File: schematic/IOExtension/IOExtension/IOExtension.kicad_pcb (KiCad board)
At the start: 2 copper layers, 73.4 x 72.4 mm, 32 parts, among them J1 Address, J10 Opto_GPB2, J11 Opto_GPB3, J12 IO_GPB, J13 Opto_GPB4, J14 OLED_SCR, J2 TTL Serial OUT, J3 PORT_C_IN, J4 PORT_C_OUT, J5 INTs/Ts, J6 TTL Serial IN, J7 INTs/Ts, J8 IO_GPA, J9 Opto_IN, U1 MCP23017_SP, U2 4N25, U3 4N25, U4 4N25

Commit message: Latest shcematic of IOExtesion board and latest Gerbers
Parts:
- added GND: MountingHole_2.2mm_M2_ISO7380_Pad, MountingHole:MountingHole_2.2mm_M2_ISO7380_Pad, F.Cu at (111.5, 108.5)
- added GND: MountingHole_2.2mm_M2_ISO7380_Pad, MountingHole:MountingHole_2.2mm_M2_ISO7380_Pad, F.Cu at (132.5, 108.5)
- added R12: 1K, Resistor_THT:R_Axial_DIN0204_L3.6mm_D1.6mm_P7.62mm_Horizontal, F.Cu at (126.0, 96.9)
- added R13: 1K, Resistor_THT:R_Axial_DIN0204_L3.6mm_D1.6mm_P7.62mm_Horizontal, F.Cu at (123.5, 96.9)
- added SW1: B_USER1, Button_Switch_THT:SW_PUSH_6mm_H5mm, F.Cu at (131.5, 73.0)
- added U5: 24LC512, Package_DIP:DIP-8_W7.62mm, F.Cu at (83.2, 94.2)
- moved J14 32.4 mm to (118.4, 87.0), turned to 90 degrees
- moved J9 6.20 mm to (136.0, 67.1)
- moved R1 5.00 mm to (102.3, 98.5)
- moved R3 5.00 mm to (102.3, 93.5)
- moved C4 3.16 mm to (106.0, 81.5)
- moved J8 2.29 mm to (138.0, 82.0)
- moved J1 1.96 mm to (101.0, 102.0)
- moved J12 1.88 mm to (73.5, 101.3)
- moved R11 1.57 mm to (117.6, 77.5)
- moved R4 1.50 mm to (85.6, 78.0)
- moved J13 1.46 mm to (84.0, 69.0)
- moved J10 1.42 mm to (89.5, 60.0)
- moved J11 1.42 mm to (89.5, 69.0)
- moved D1 1.27 mm to (72.8, 78.0)
- moved U4 1.22 mm to (117.7, 69.5)
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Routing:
- net /SCK: track 61.2 -> 101.8 mm, vias 1 -> 2
- net /SDA: track 66.6 -> 104.6 mm
- net Net-(J8-Pin_1): track 53.1 -> 64.1 mm
- net +5V: track 320.9 -> 329.8 mm
- net Net-(J9-Pin_1): track 31.7 -> 38.5 mm
- net Net-(J1-Pin_5): track 19.4 -> 15.8 mm
- net /GPB3_OPTO: track 51.5 -> 54.4 mm
- net Net-(J1-Pin_3): track 21.1 -> 18.3 mm
- net Net-(J1-Pin_1): track 23.0 -> 20.4 mm
- net Net-(J9-Pin_3): track 29.4 -> 27.0 mm
- net /GPB4_DIR: track 39.6 -> 37.2 mm
- net Net-(J8-Pin_8): track 46.9 -> 49.2 mm
- net /GPB7: track 38.3 -> 36.5 mm
- net /GPB6: track 38.3 -> 36.6 mm
- net Net-(J9-Pin_4): track 45.2 -> 46.9 mm
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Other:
- board size 73.4 x 72.4 mm -> 73.4 x 71.4 mm
- board text added: "+VDC IN"
- board text added: "AREF"
- board text added: "GND"
- board text added: "SCL"
- board text added: "SDA"
- board text added: "VCC"
- board text removed: "+VDC"

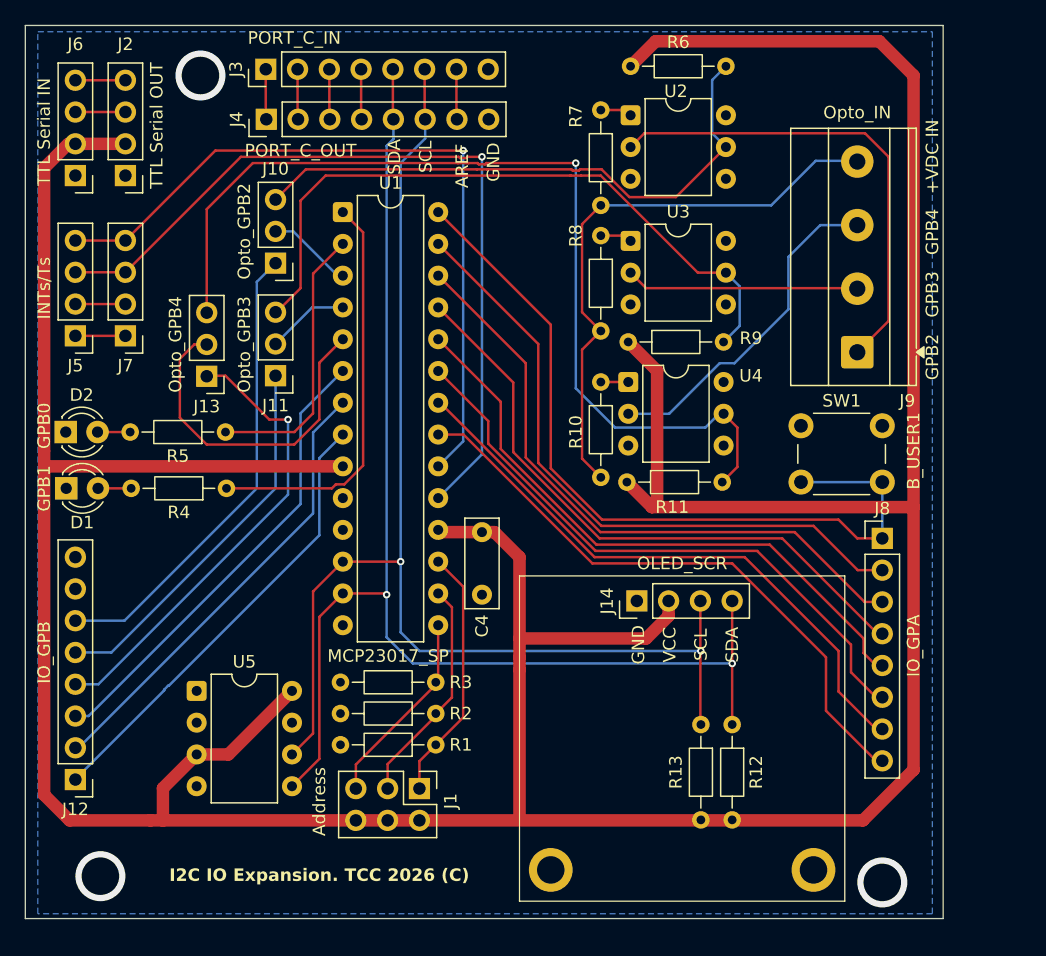
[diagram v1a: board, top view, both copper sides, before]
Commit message: Latest schematic of IOExtension modifications
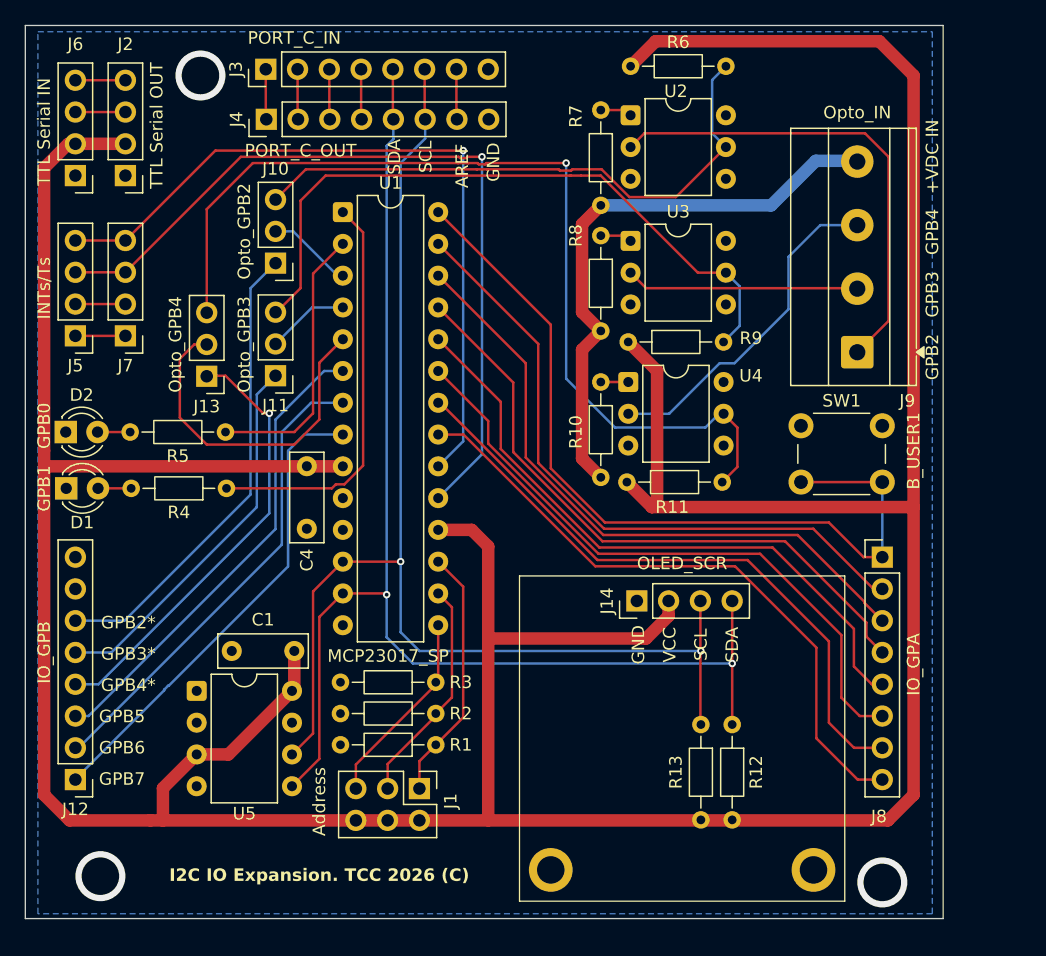
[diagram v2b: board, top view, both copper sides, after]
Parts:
- added C1: 100nF, Capacitor_THT:C_Disc_D7.0mm_W2.5mm_P5.00mm, F.Cu at (91.0, 91.0)
- moved C4 15.0 mm to (92.0, 76.2)
- moved J8 1.50 mm to (138.0, 83.5)
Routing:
- net +5V: track 329.8 -> 334.8 mm
- net Net-(J8-Pin_7): track 48.3 -> 50.7 mm
- net Net-(J8-Pin_8): track 49.2 -> 51.4 mm
- net Net-(J8-Pin_1): track 64.1 -> 66.2 mm
- net Net-(J8-Pin_6): track 49.0 -> 51.0 mm
- net /GPB4_DIR: track 37.2 -> 35.4 mm
- net Net-(J8-Pin_4): track 49.1 -> 50.9 mm
- net /GPB7: track 36.5 -> 38.3 mm
- net Net-(J8-Pin_5): track 49.6 -> 51.1 mm
- net /GPB6: track 36.6 -> 38.1 mm
- net /GPB5: track 37.1 -> 37.9 mm
- net Net-(J8-Pin_3): track 50.7 -> 51.4 mm
- net Net-(J8-Pin_2): track 51.9 -> 52.5 mm
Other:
- board text added: "GPB2*"
- board text added: "GPB3*"
- board text added: "GPB4*"
- board text added: "GPB5"
- board text added: "GPB6"
- board text added: "GPB7"
